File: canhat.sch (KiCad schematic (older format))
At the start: 36 parts, among them J1 Raspberry_Pi_2_3, J2 CAN In/Out/GND, J5 12V, U1 MCP2515-xSO, U2 SN65HVD234, U3 AT24C32-SSHM, U4 AP63205, Y1 16MHz

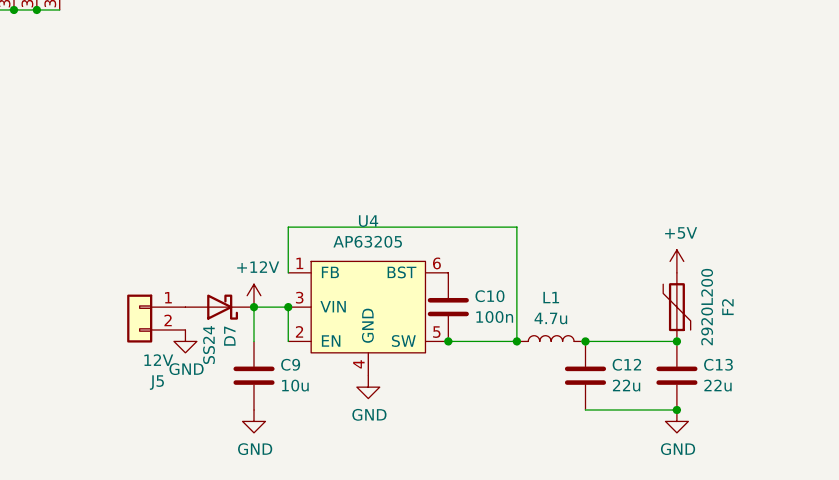
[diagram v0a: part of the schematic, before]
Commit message: Added direct-5V jumper
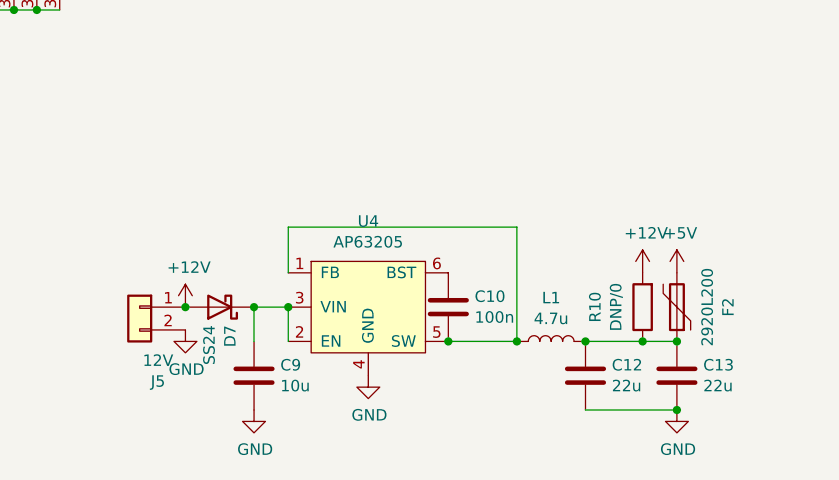
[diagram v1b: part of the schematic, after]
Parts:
- added R10: DNP/0, Resistor_SMD:R_0805_2012Metric_Pad1.15x1.40mm_HandSolder, symbol Device:R
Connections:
- net +12V: now also D7.2 (A), J5.1 (Pin_1), R10.2; no longer C9.1, D7.1 (K), U4.2 (EN), U4.3 (VIN)
- net at C12.1, C13.1, F2.1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: now also R10.1
- new net: C9.1, D7.1 (K), U4.2 (EN), U4.3 (VIN)
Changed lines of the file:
@@
 L power:+12V #PWR07
 U 1 1 5DC9A6CE
-P 3200 6700
-F 0 "#PWR07" H 3200 6550 50  0001 C CNN
-F 1 "+12V" H 3215 6873 50  0000 C CNN
-F 2 "" H 3200 6700 50  0001 C CNN
-F 3 "" H 3200 6700 50  0001 C CNN
-	1    3200 6700
+P 2900 6700
+F 0 "#PWR07" H 2900 6550 50  0001 C CNN
+F 1 "+12V" H 2915 6873 50  0000 C CNN
+F 2 "" H 2900 6700 50  0001 C CNN
+F 3 "" H 2900 6700 50  0001 C CNN
+	1    2900 6700
 	1    0    0    -1
 $EndComp
@@
 $EndComp
 Wire Wire Line
-	5050 6850 4650 6850
+	5050 6850 4900 6850
 Connection ~ 4650 6850
 Wire Wire Line
@@
 	1    0    0    -1
 $EndComp
+$Comp
+L Device:R R10
+U 1 1 5DCDF172
+P 4900 6700
+F 0 "R10" V 5107 6700 50  0000 C CNN
+F 1 "DNP/0" V 5016 6700 50  0000 C CNN
+F 2 "Resistor_SMD:R_0805_2012Metric_Pad1.15x1.40mm_HandSolder" V 4830 6700 50  0001 C CNN
+F 3 "~" H 4900 6700 50  0001 C CNN
+	1    4900 6700
+	-1   0    0    1
+$EndComp
+Connection ~ 4900 6850
+Wire Wire Line
+	4900 6850 4650 6850
+$Comp
+L power:+12V #PWR0114
+U 1 1 5DCDFA49
+P 4900 6550
+F 0 "#PWR0114" H 4900 6400 50  0001 C CNN
+F 1 "+12V" H 4915 6723 50  0000 C CNN
+F 2 "" H 4900 6550 50  0001 C CNN
+F 3 "" H 4900 6550 50  0001 C CNN
+	1    4900 6550
+	1    0    0    -1
+$EndComp
+Connection ~ 2900 6700
 $EndSCHEMATC

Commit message: Fine tuning
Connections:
- net +3V3: no longer J1.1 (3V3)
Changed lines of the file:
@@
 	1    0    0    -1
 $EndComp
-Wire Wire Line
-	2250 2800 2150 2800
-Connection ~ 2250 2800
 Text Label 4750 3300 2    50   ~ 0
 MISO

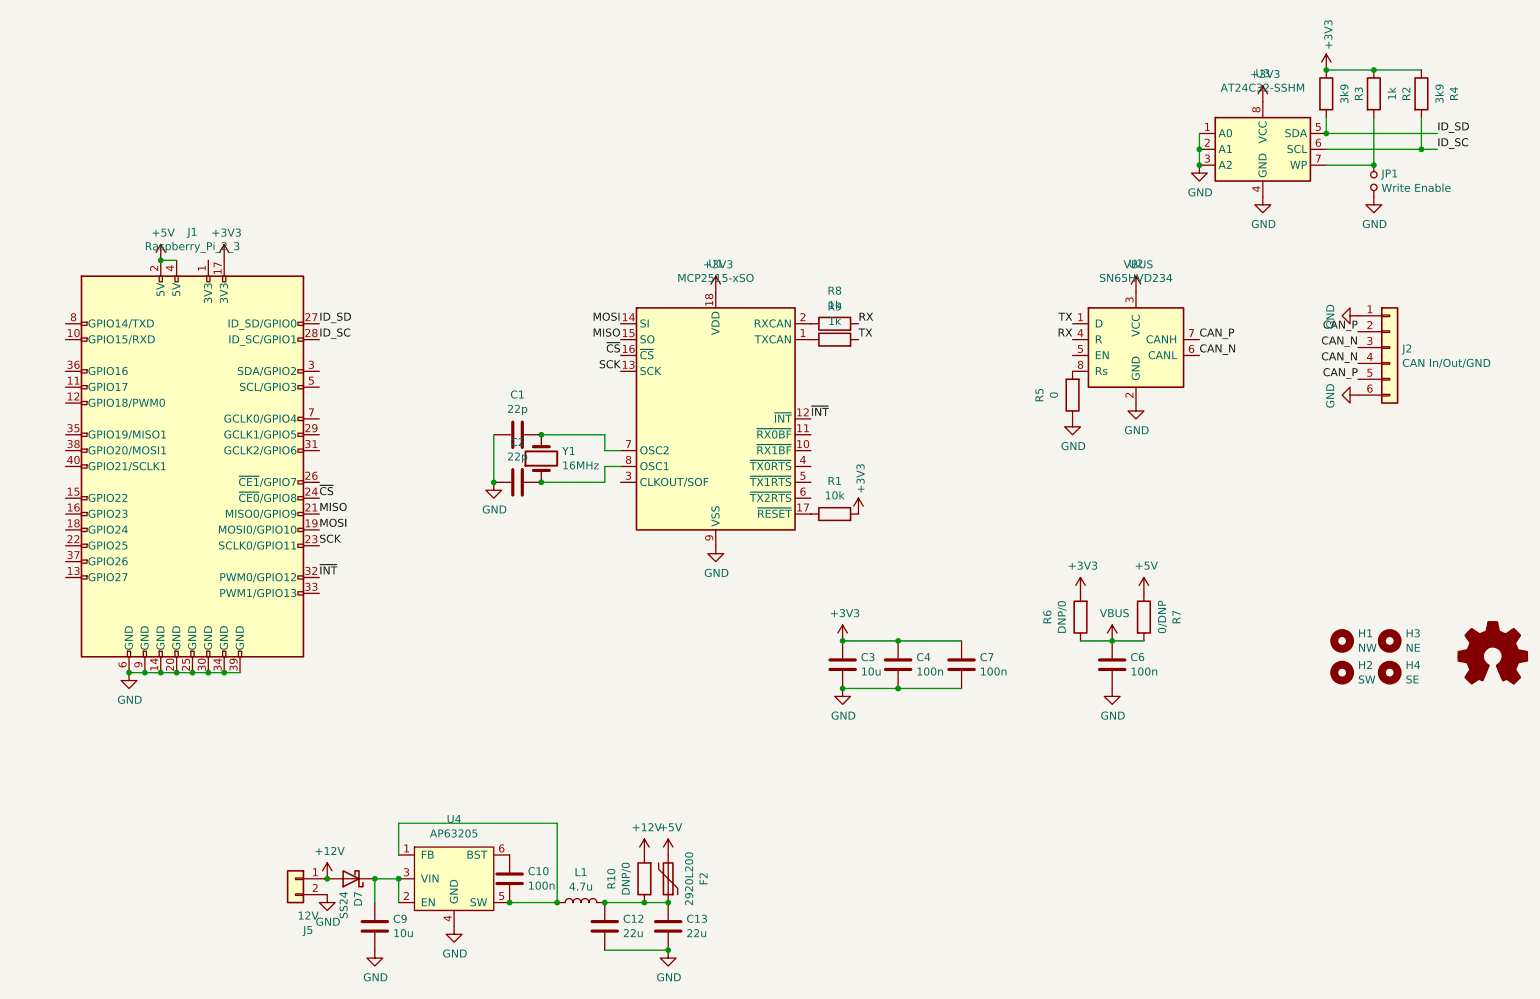
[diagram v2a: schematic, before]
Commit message: Added front ground to optimize dissipation
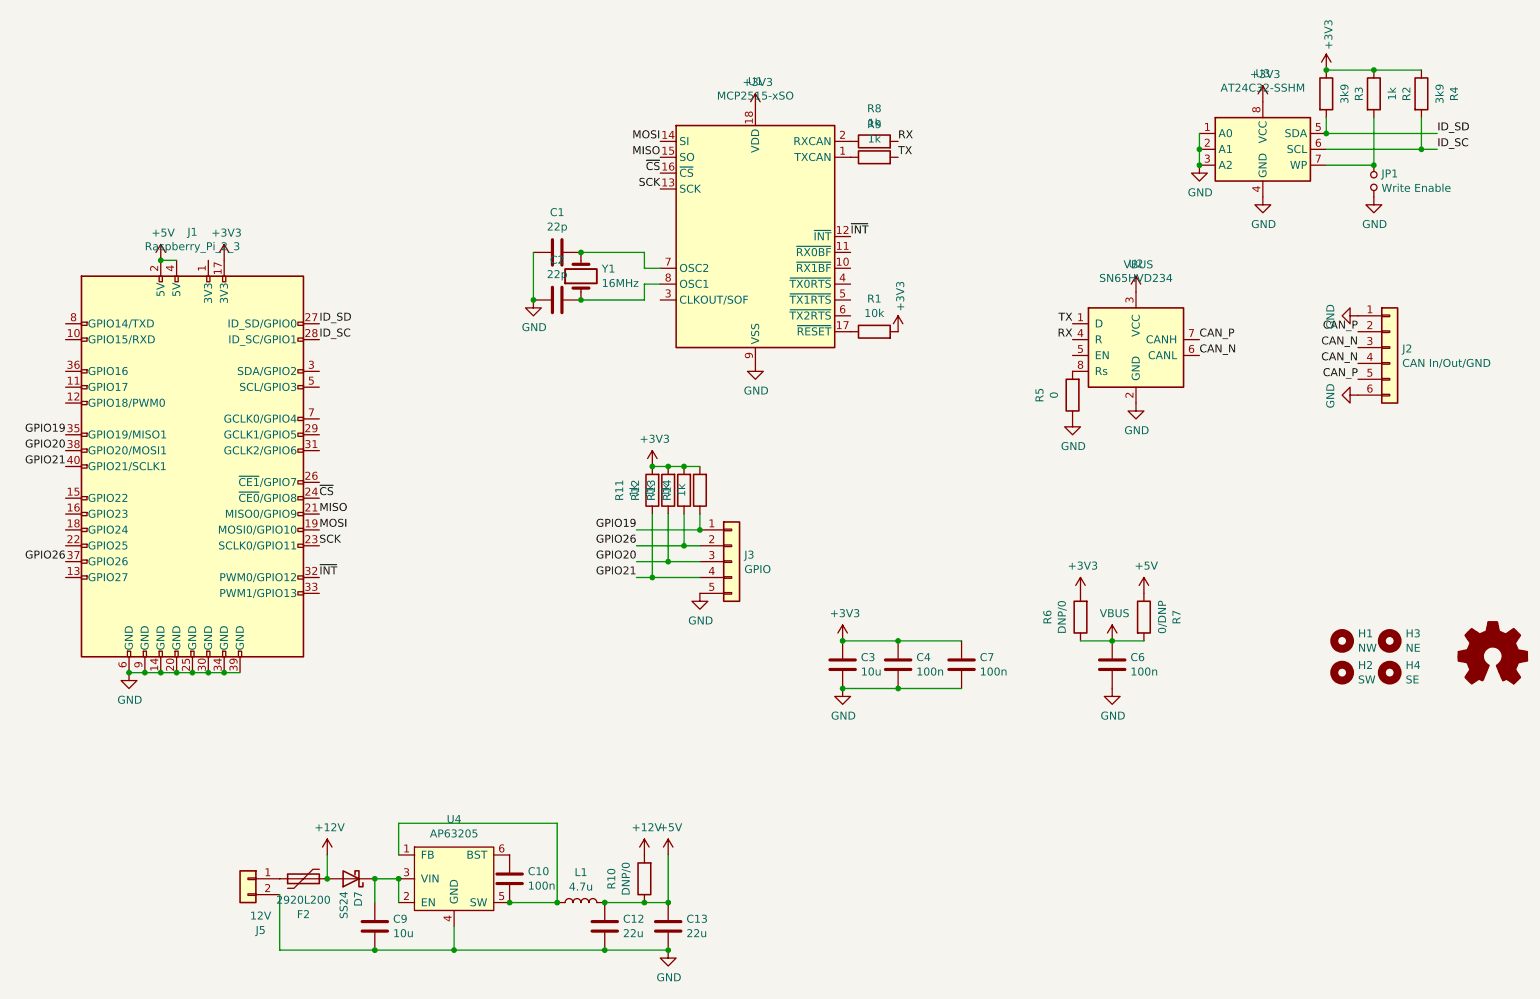
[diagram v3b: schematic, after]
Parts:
- added J3: GPIO, Connector_PinHeader_2.54mm:PinHeader_1x05_P2.54mm_Vertical, symbol Connector_Generic:Conn_01x05
- added R11, R12, R13, R14: 1k, Resistor_SMD:R_0805_2012Metric_Pad1.15x1.40mm_HandSolder, symbol Device:R
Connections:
- net +12V: now also F2.2; no longer J5.1 (Pin_1)
- net +3V3: now also R11.2, R12.2, R13.2, R14.2
- net +5V: now also C12.1, C13.1, L1.2, R10.1; no longer F2.2
- net GND: now also J3.5 (Pin_5)
- net GPIO19: now reaches J1.35 (GPIO19/MISO1)
- net GPIO19: now also J3.1 (Pin_1), R14.1
- net GPIO26: now reaches J1.37 (GPIO26)
- net GPIO26: now also J3.2 (Pin_2), R13.1
- net GPIO20: now reaches J1.38 (GPIO20/MOSI1)
- net GPIO20: now also J3.3 (Pin_3), R12.1
- net GPIO21: now reaches J1.40 (GPIO21/SCLK1)
- net GPIO21: now also J3.4 (Pin_4), R11.1
- new net: F2.1, J5.1 (Pin_1)
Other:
- moved on the sheet: C1, C2, F2, J5, R1, R8, R9, U1, Y1

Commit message: Replaced input cap with 0805
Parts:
- C9: footprint Capacitor_SMD:C_1210_3225Metric_Pad1.42x2.65mm_HandSolder -> Capacitor_SMD:C_0805_2012Metric_Pad1.15x1.40mm_HandSolder
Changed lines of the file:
@@
 F 0 "C9" H 3315 7046 50  0000 L CNN
 F 1 "10u" H 3315 6955 50  0000 L CNN
-F 2 "Capacitor_SMD:C_1210_3225Metric_Pad1.42x2.65mm_HandSolder" H 3238 6850 50  0001 C CNN
+F 2 "Capacitor_SMD:C_0805_2012Metric_Pad1.15x1.40mm_HandSolder" H 3238 6850 50  0001 C CNN
 F 3 "~" H 3200 7000 50  0001 C CNN
 	1    3200 7000

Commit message: Added GPIO pullups
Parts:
- C3: footprint Capacitor_SMD:C_1210_3225Metric_Pad1.42x2.65mm_HandSolder -> Capacitor_SMD:C_0805_2012Metric_Pad1.15x1.40mm_HandSolder
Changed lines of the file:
@@
 Date "2019-11-12"
 Rev "5"
-Comp "© 2019 Gregor Riepl"
+Comp "© 2020 Gregor Riepl"
 Comment1 ""
 Comment2 ""
@@
 F 0 "C3" H 6265 5396 50  0000 L CNN
 F 1 "10u" H 6265 5305 50  0000 L CNN
-F 2 "Capacitor_SMD:C_1210_3225Metric_Pad1.42x2.65mm_HandSolder" H 6188 5200 50  0001 C CNN
+F 2 "Capacitor_SMD:C_0805_2012Metric_Pad1.15x1.40mm_HandSolder" H 6188 5200 50  0001 C CNN
 F 3 "~" H 6150 5350 50  0001 C CNN
 	1    6150 5350

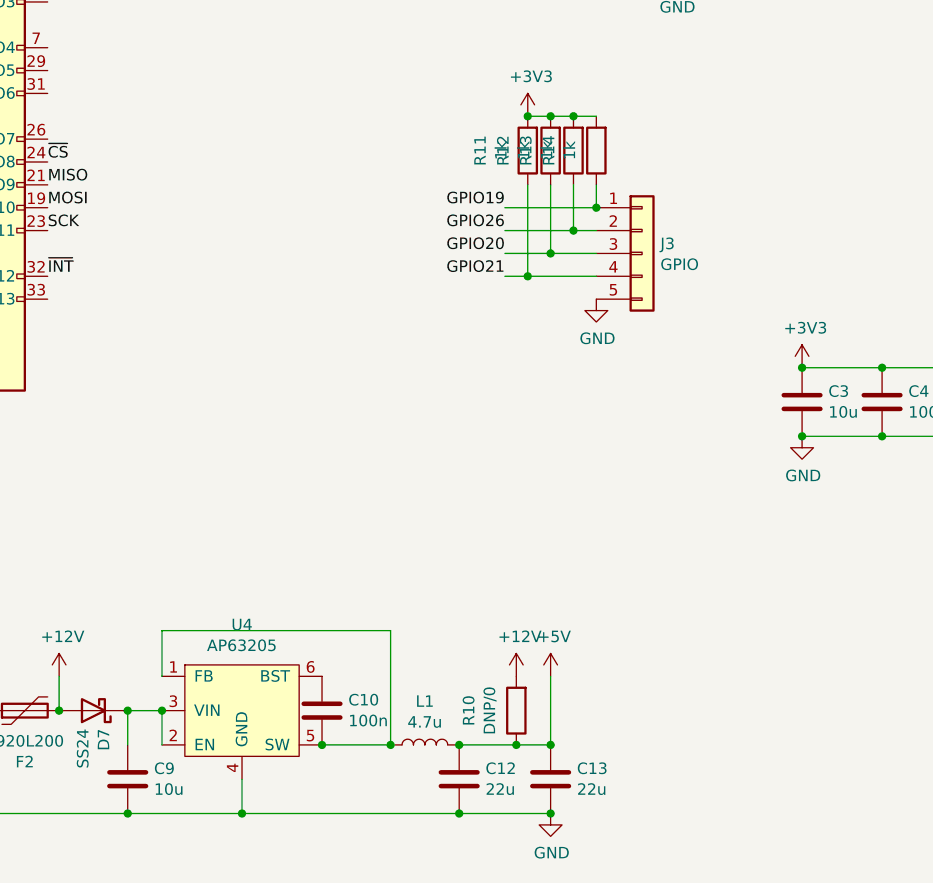
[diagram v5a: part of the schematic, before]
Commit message: Fixed incorrect feedback pin wire
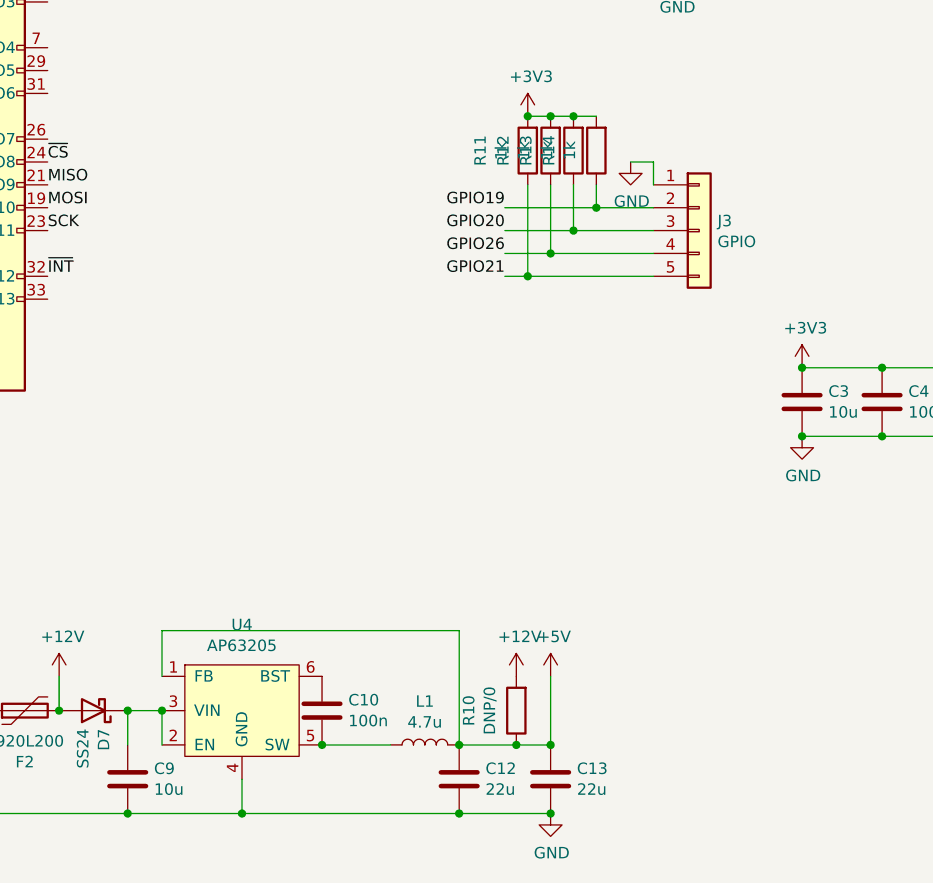
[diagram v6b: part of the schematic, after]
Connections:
- net +5V: now also U4.1 (FB)
- net GND: now also J3.1 (Pin_1); no longer J3.5 (Pin_5)
- net GPIO19: now also J3.2 (Pin_2); no longer J3.1 (Pin_1)
- net GPIO20: now also R13.1; no longer R12.1
- net GPIO21: now also J3.5 (Pin_5); no longer J3.4 (Pin_4)
- net GPIO26: now also J3.4 (Pin_4), R12.1; no longer J3.2 (Pin_2), R13.1
- net at C10.2, L1.1, U4.5 (SW): no longer U4.1 (FB)
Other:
- moved on the sheet: J3
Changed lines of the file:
@@
 	4050 6850 4350 6850
 Wire Wire Line
-	4350 6850 4350 6350
-Wire Wire Line
-	4350 6350 3350 6350
-Wire Wire Line
 	3350 6350 3350 6550
-Connection ~ 4350 6850
 $Comp
 L Device:Polyfuse F2
@@
 $EndComp
 $Comp
-L Connector_Generic:Conn_01x05 J3
-U 1 1 5DDDB345
-P 5450 4700
-F 0 "J3" H 5530 4742 50  0000 L CNN
-F 1 "GPIO" H 5530 4651 50  0000 L CNN
-F 2 "Connector_PinHeader_2.54mm:PinHeader_1x05_P2.54mm_Vertical" H 5450 4700 50  0001 C CNN
-F 3 "~" H 5450 4700 50  0001 C CNN
-	1    5450 4700
-	1    0    0    -1
-$EndComp
-$Comp
 L Device:R R14
 U 1 1 5DDFEBFA
@@
 	5150 4400 5150 4600
 Wire Wire Line
-	5150 4600 5250 4600
-Wire Wire Line
 	5050 4400 5050 4700
 Wire Wire Line
-	5050 4700 5250 4700
-Wire Wire Line
 	4950 4400 4950 4800
 Wire Wire Line
-	4950 4800 5250 4800
-Wire Wire Line
 	5250 4500 4850 4500
-Connection ~ 5250 4500
 Wire Wire Line
 	5150 4600 4850 4600
@@
 	4950 4800 4850 4800
 Connection ~ 4950 4800
-$Comp
-L power:GND #PWR0112
-U 1 1 5DE13DE3
-P 5250 4900
-F 0 "#PWR0112" H 5250 4650 50  0001 C CNN
-F 1 "GND" H 5255 4727 50  0000 C CNN
-F 2 "" H 5250 4900 50  0001 C CNN
-F 3 "" H 5250 4900 50  0001 C CNN
-	1    5250 4900
-	1    0    0    -1
-$EndComp
 Text Label 1250 3900 2    50   ~ 0
 GPIO19
@@
 Text Label 4850 4500 2    50   ~ 0
 GPIO19
+Text Label 4850 4700 2    50   ~ 0
+GPIO26
 Text Label 4850 4600 2    50   ~ 0
-GPIO26
-Text Label 4850 4700 2    50   ~ 0
 GPIO20
 Text Label 4850 4800 2    50   ~ 0
@@
 	1    0    0    -1
 $EndComp
+Connection ~ 5250 4500
+$Comp
+L Connector_Generic:Conn_01x05 J3
+U 1 1 5DDDB345
+P 5700 4600
+F 0 "J3" H 5780 4642 50  0000 L CNN
+F 1 "GPIO" H 5780 4551 50  0000 L CNN
+F 2 "Connector_PinHeader_2.54mm:PinHeader_1x05_P2.54mm_Vertical" H 5700 4600 50  0001 C CNN
+F 3 "~" H 5700 4600 50  0001 C CNN
+	1    5700 4600
+	1    0    0    -1
+$EndComp
+Wire Wire Line
+	5250 4500 5500 4500
+Wire Wire Line
+	5150 4600 5500 4600
+Wire Wire Line
+	5050 4700 5500 4700
+Wire Wire Line
+	4950 4800 5500 4800
+$Comp
+L power:GND #PWR0112
+U 1 1 5DE13DE3
+P 5400 4300
+F 0 "#PWR0112" H 5400 4050 50  0001 C CNN
+F 1 "GND" H 5405 4127 50  0000 C CNN
+F 2 "" H 5400 4300 50  0001 C CNN
+F 3 "" H 5400 4300 50  0001 C CNN
+	1    5400 4300
+	1    0    0    -1
+$EndComp
+Wire Wire Line
+	5500 4400 5500 4300
+Wire Wire Line
+	5500 4300 5400 4300
+Wire Wire Line
+	4650 6350 4650 6850
+Wire Wire Line
+	3350 6350 4650 6350
 $EndSCHEMATC
